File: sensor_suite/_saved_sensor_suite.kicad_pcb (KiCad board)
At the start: 4 copper layers, 12 parts, among them J1 Conn_01x02, J2 Conn_01x02, J3 Bar02, J4 LSM303, U3 MAX6581, U4 ADuM1250, U5 LM3480-3.3

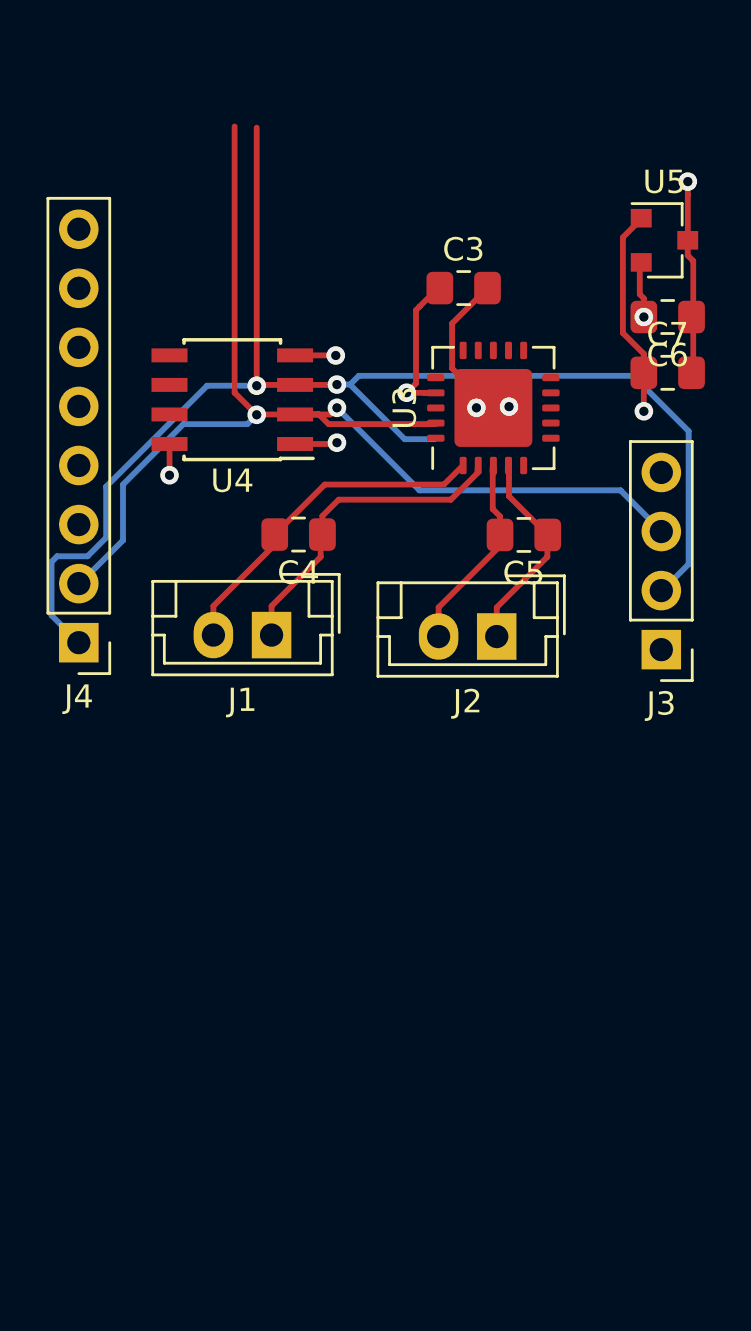
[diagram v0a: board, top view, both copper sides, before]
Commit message: PCA symbol moved to sensor board
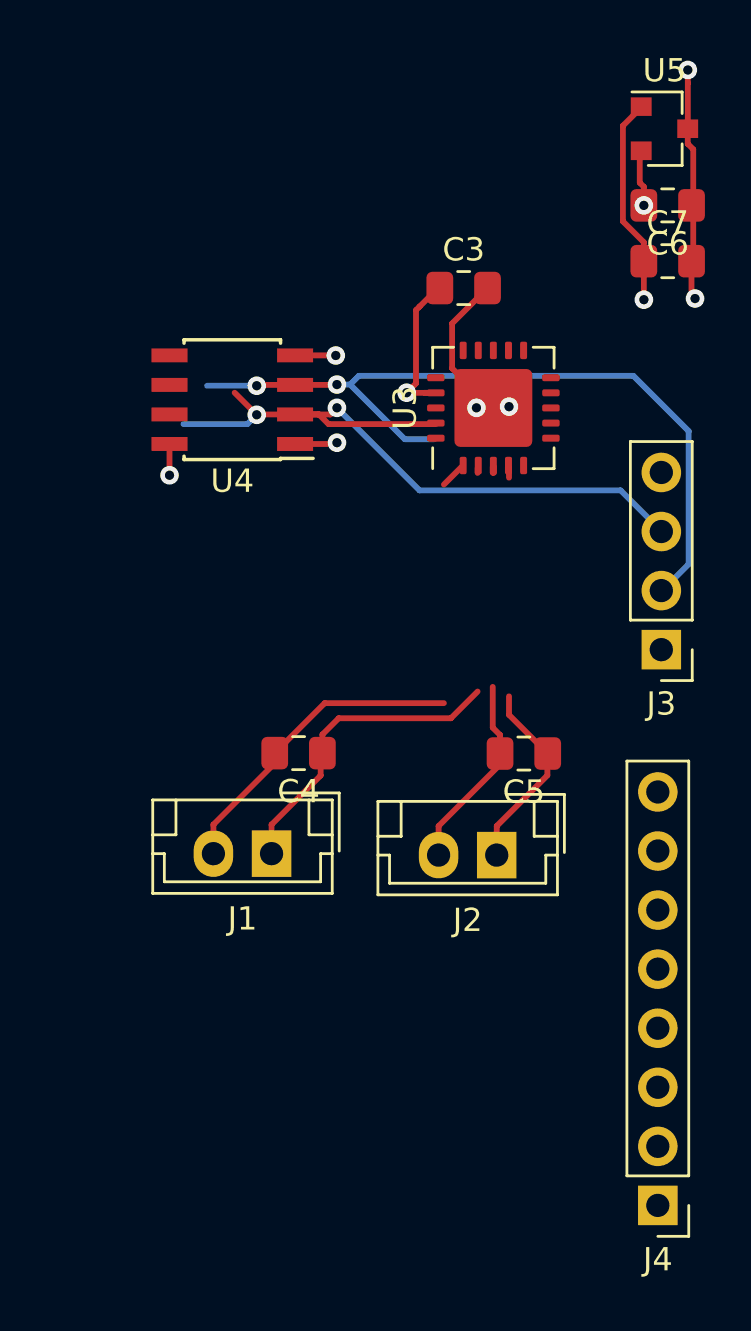
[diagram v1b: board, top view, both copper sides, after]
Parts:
- moved J4 34.7 mm to (170.2, 126.0)
- moved C5 9.40 mm to (164.4, 106.6)
- moved J1 9.40 mm to (153.6, 110.9)
- moved C4 9.40 mm to (154.8, 106.5)
- moved J2 9.40 mm to (163.3, 110.9)
- moved U5 4.80 mm to (170.5, 79.7)
- moved C6 4.80 mm to (170.6, 83.0)
- moved C7 4.80 mm to (170.6, 85.4)
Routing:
- net /SCL1: track 60.0 -> 33.9 mm
- net /SDA1: track 50.9 -> 30.7 mm
- net GND: track 8.47 -> 10.1 mm, vias 1 -> 2

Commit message: updated library
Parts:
- removed C6, C7: 0.1uF, Capacitor_SMD:C_0805_2012Metric_Pad1.15x1.40mm_HandSolder
- removed U3: MAX6581, Package_DFN_QFN:QFN-20-1EP_5x5mm_P0.65mm_EP3.35x3.35mm
- removed U4: ADuM1250, Package_SO:SOIC-8_3.9x4.9mm_P1.27mm
- removed U5: LM3480-3.3, Package_TO_SOT_SMD:SOT-23
- added C1: 100pF, Capacitor_SMD:C_0805_2012Metric_Pad1.15x1.40mm_HandSolder, F.Cu at (122.7, 115.8)
- added C2: 100pF, Capacitor_SMD:C_0805_2012Metric_Pad1.15x1.40mm_HandSolder, F.Cu at (132.7, 115.6)
- added J5: LSM303, rov:LSM303, F.Cu at (94.2, 122.5)
- added U1: MAX6581, Package_DFN_QFN:QFN-20-1EP_5x5mm_P0.65mm_EP3.35x3.35mm, F.Cu at (131.5, 109.1)
- added U2: LM3480-3.3, Package_TO_SOT_SMD:SOT-23, F.Cu at (117.8, 110.1)
- C4, C5: value 100pF -> 0.1uF
- J1: value Conn_01x02 -> Bar02; footprint Connector_JST:JST_EH_B02B-EH-A_1x02_P2.50mm_Vertical -> Connector_PinHeader_2.54mm:PinHeader_1x04_P2.54mm_Vertical
- J2: value Conn_01x02 -> Conn_02x15_Top_Bottom; footprint Connector_JST:JST_EH_B02B-EH-A_1x02_P2.50mm_Vertical -> rov:PCA9685
- J3: value Bar02 -> Conn_01x02; footprint Connector_PinHeader_2.54mm:PinHeader_1x04_P2.54mm_Vertical -> Connector_JST:JST_EH_B02B-EH-A_1x02_P2.50mm_Vertical
- J4: value LSM303 -> Conn_01x02; footprint Connector_PinHeader_2.54mm:PinHeader_1x08_P2.54mm_Vertical -> Connector_JST:JST_EH_B02B-EH-A_1x02_P2.50mm_Vertical
- moved J2 64.2 mm to (105.2, 83.5), turned to 0 degrees
- moved J3 52.3 mm to (121.5, 120.8)
- moved C5 41.3 mm to (123.3, 110.3), turned to 90 degrees
- moved J4 39.1 mm to (131.5, 120.8)
- moved C3 36.2 mm to (130.1, 103.9)
- moved C4 33.9 mm to (121.1, 110.1), turned to 270 degrees
- moved J1 16.2 mm to (137.6, 113.6), turned to 0 degrees
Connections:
- C4 pad 1: /temp1p -> GNDPWR
- C4 pad 2: /temp1n -> +5VP
- C5 pad 1: /temp2p -> +3V3
- C5 pad 2: /temp2n -> GNDPWR
- J1 pad 1: /temp1p -> +3V3
- J1 pad 2: /temp1n -> /SCL_iso
- J2 pad 1: /temp2p -> GND
- J2 pad 2: /temp2n -> Net-(J2-Pad2)
- J3 pad 1: +3V3 -> /temp1p
- J3 pad 2: /SCL1 -> /temp1n
- J4 pad 1: /SCL1 -> /temp2p
- J4 pad 2: /SDA1 -> /temp2n
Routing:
- net +3V3: track 17.6 -> 74.3 mm, vias 3 -> 0
- net /SCL1: track 33.9 -> 0.00 mm, vias 2 -> 0
- net /SDA1: track 30.7 -> 0.00 mm, vias 2 -> 0
- net GND: track 10.1 -> 0.00 mm, vias 2 -> 0
- net GNDPWR: track 0.00 -> 10.1 mm, vias 0 -> 2
- net +12P: track 2.42 -> 0.00 mm, vias 1 -> 0
- net /temp2p: track 9.04 -> 10.9 mm
- net GNDS: track 6.96 -> 5.21 mm, vias 3 -> 2
- net /temp2n: track 8.94 -> 10.7 mm
- net /temp1n: track 14.7 -> 16.4 mm
- net /temp1p: track 13.7 -> 15.0 mm
- net +5VP: track 1.34 -> 2.42 mm
- removed copper zone on power.Cu, net +12P
- removed copper zone on power.Cu, net +3V3
- removed copper zone on power.Cu, net +5VP
- removed copper zone on ground.Cu, net GND
- removed copper zone on ground.Cu, net GNDS

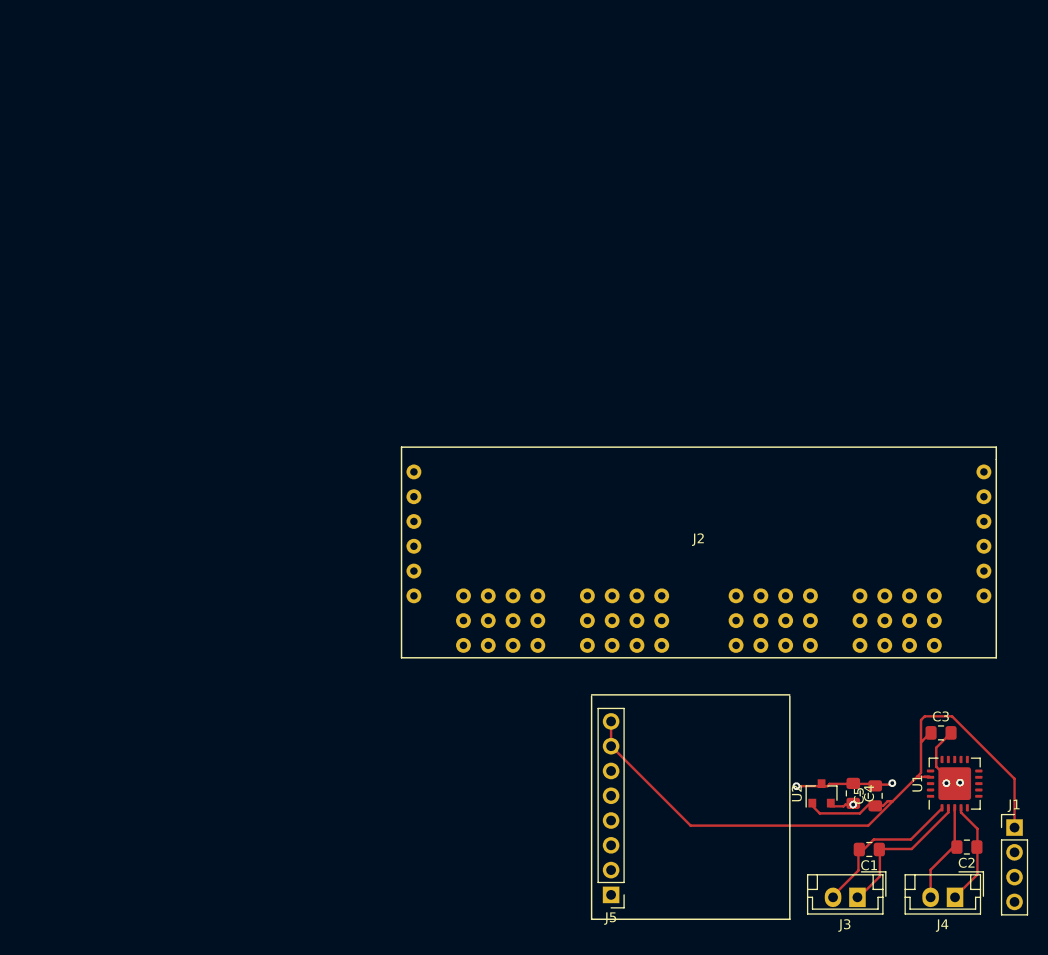
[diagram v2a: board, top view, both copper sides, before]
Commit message: updated ESC's
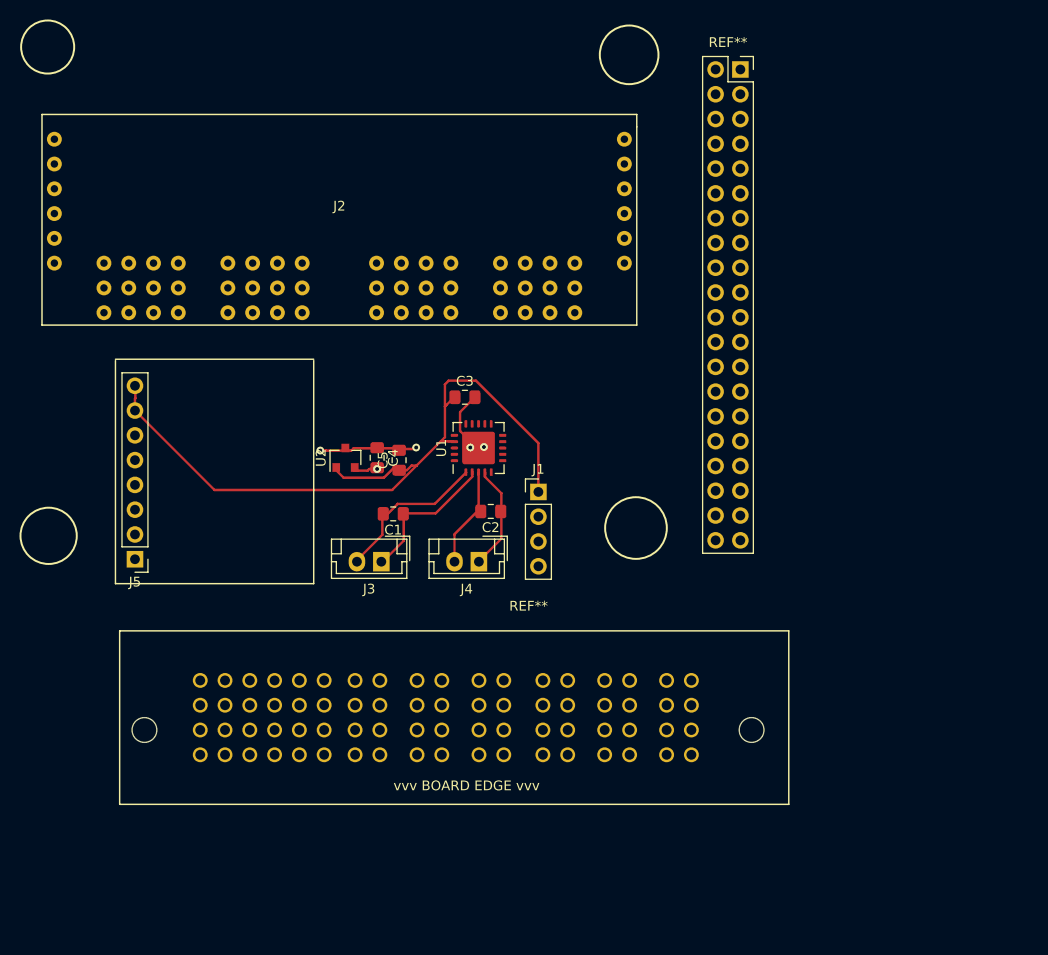
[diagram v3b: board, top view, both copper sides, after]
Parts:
- added REF**: 609-3634-ND, rov:609-3634-ND, F.Cu at (48.4, 98.5)
- added REF**: PinSocket_2x20_P2.54mm_Vertical, Connector_PinSocket_2.54mm:PinSocket_2x20_P2.54mm_Vertical, F.Cu at (109.5, 35.9)
- moved C3 59.7 mm to (81.3, 69.5)
- moved C4 59.7 mm to (72.3, 75.7)
- moved C5 59.7 mm to (74.5, 75.9)
- moved J3 59.7 mm to (72.7, 86.3)
- moved J4 59.7 mm to (82.7, 86.3)
- moved J5 59.7 mm to (45.5, 88.1)
- moved U2 59.7 mm to (69.0, 75.7)
- moved C1 59.7 mm to (73.9, 81.4)
- moved C2 59.7 mm to (83.9, 81.2)
- moved J1 59.7 mm to (88.8, 79.2)
- moved U1 59.7 mm to (82.7, 74.7)
- moved J2 50.2 mm to (68.4, 49.4)

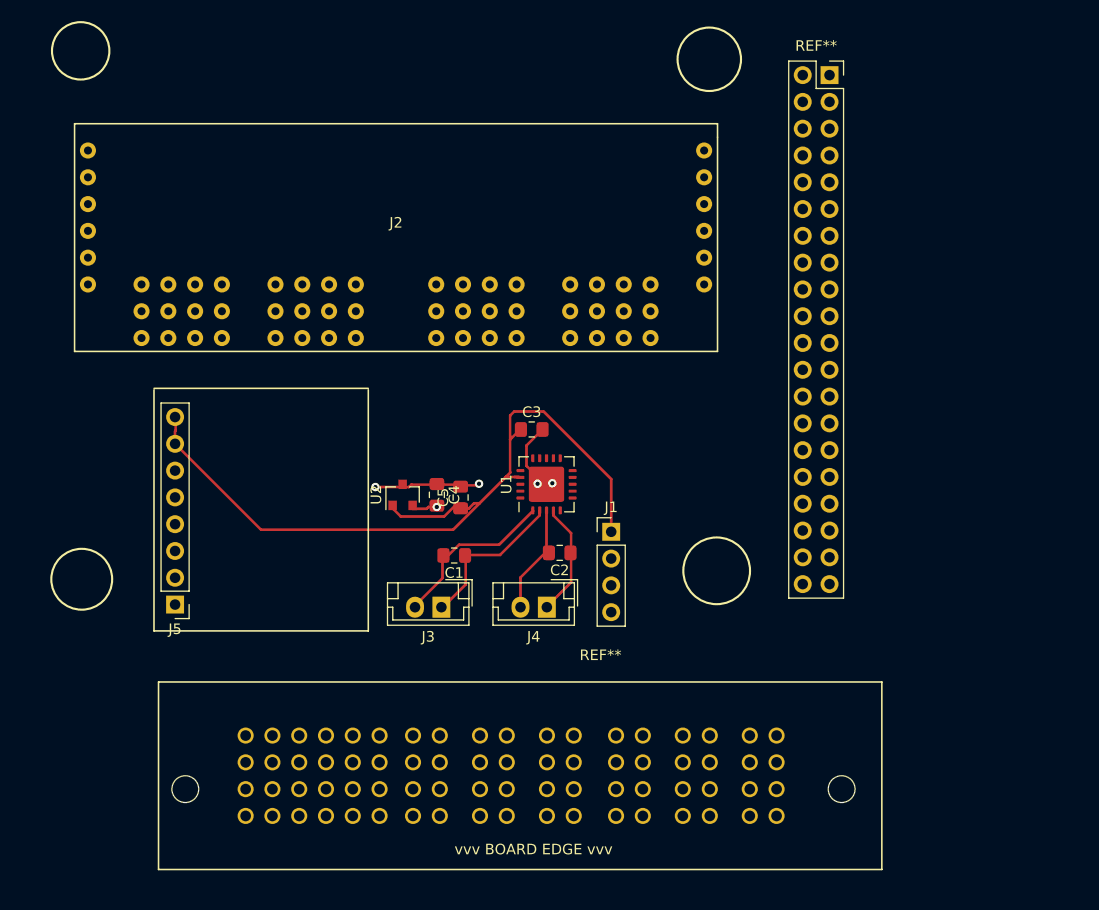
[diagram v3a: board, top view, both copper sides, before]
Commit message: sensors unrouted
nick look in "sensor suite"
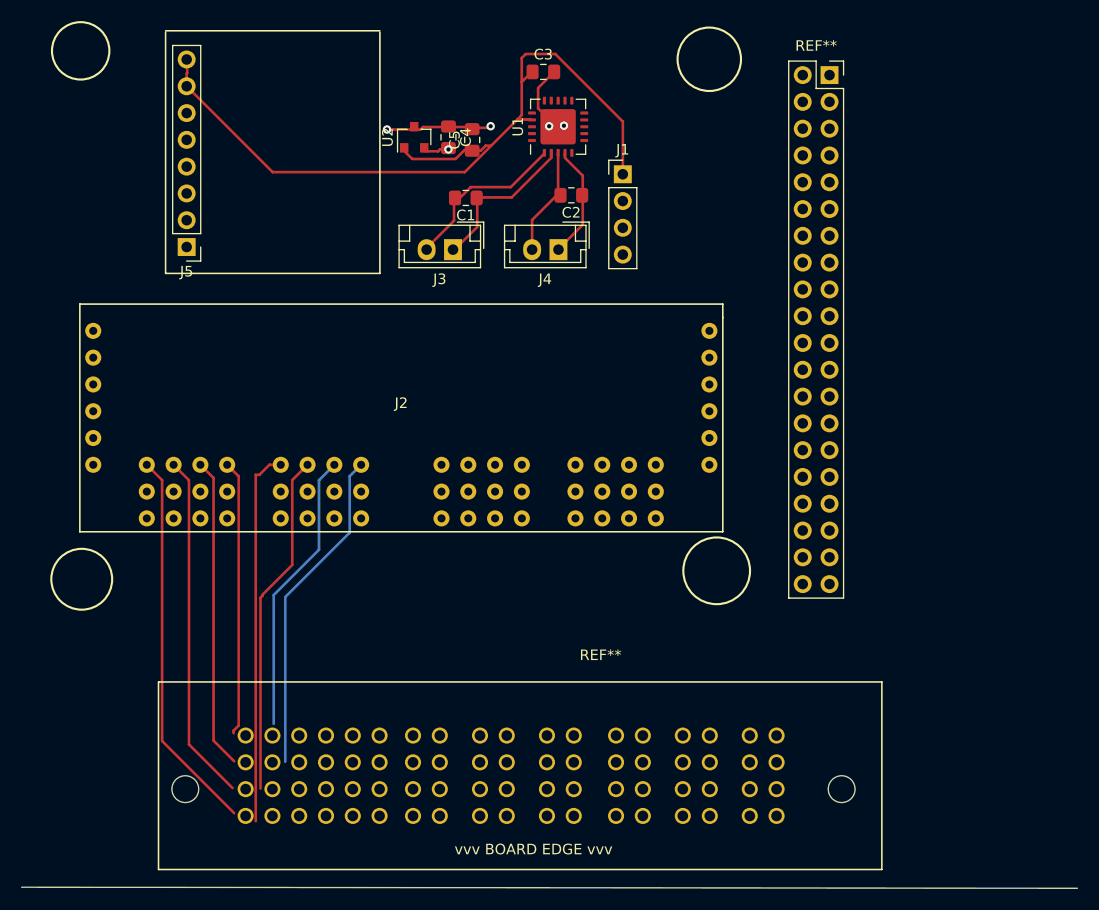
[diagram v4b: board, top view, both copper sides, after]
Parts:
- moved C1 33.9 mm to (75.0, 47.5)
- moved C2 33.9 mm to (85.0, 47.3)
- moved J1 33.9 mm to (89.9, 45.3)
- moved U1 33.9 mm to (83.8, 40.8)
- moved C3 33.9 mm to (82.4, 35.6)
- moved C4 33.9 mm to (73.4, 41.8)
- moved C5 33.9 mm to (75.6, 42.0)
- moved J3 33.9 mm to (73.8, 52.5)
- moved J4 33.9 mm to (83.8, 52.5)
- moved J5 33.9 mm to (46.5, 54.2)
- moved U2 33.9 mm to (70.1, 41.8)
- moved J2 17.1 mm to (68.9, 66.5)
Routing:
- net /PWM5: track 0.00 -> 90.6 mm
- net /PWM0: track 0.00 -> 36.5 mm
- net /PWM4: track 0.00 -> 35.6 mm
- net /PWM1: track 0.00 -> 33.0 mm
- net /PWM2: track 0.00 -> 29.4 mm
- net /PWM3: track 0.00 -> 26.1 mm
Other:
- board outline added: 100.1 x 0.1 mm

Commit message: Sensor Board
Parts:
- removed REF**: 609-3634-ND, rov:609-3634-ND
- removed REF**: PinSocket_2x20_P2.54mm_Vertical, Connector_PinSocket_2.54mm:PinSocket_2x20_P2.54mm_Vertical
- added CN1: 609-3634-ND, ROV:609-3634-ND, F.Cu at (129.9, 141.1)
- added J6: Conn_02x20_Counter_Clockwise, Connector_PinHeader_2.54mm:PinHeader_2x20_P2.54mm_Vertical, F.Cu at (196.5, 83.7)
- J2: value Conn_02x15_Top_Bottom -> Conn_02x10_Counter_Clockwise; footprint rov:PCA9685 -> ROV:PCA9685
- J5: footprint rov:LSM303 -> Connector_PinHeader_2.54mm:PinHeader_1x08_P2.54mm_Vertical
- moved U2 129.2 mm to (182.8, 105.2), turned to 270 degrees
- moved C4 122.0 mm to (177.5, 105.4), turned to 90 degrees
- moved C5 117.8 mm to (174.9, 105.4), turned to 270 degrees
- moved C3 114.0 mm to (168.7, 110.0), turned to 180 degrees
- moved C1 112.7 mm to (176.2, 97.2), turned to 0 degrees
- moved J3 106.8 mm to (175.5, 85.0), turned to 0 degrees
- moved U1 104.4 mm to (166.8, 104.1), turned to 270 degrees
- moved J2 102.5 mm to (158.5, 116.3)
- moved C2 95.6 mm to (166.2, 97.9), turned to 0 degrees
- moved J1 88.5 mm to (159.1, 100.5), turned to 180 degrees
- moved J4 88.2 mm to (165.8, 84.9), turned to 0 degrees
- moved J5 87.8 mm to (129.5, 83.0), turned to 0 degrees
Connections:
- J2 pad 1: GND -> PWM_0
- J2 pad 10: /PWM1 -> PWM_9
- J2 pad 11: +5VP -> PWM_10
- J2 pad 12: GNDPWR -> PWM_11
- J2 pad 13: /PWM2 -> PWM_12
- J2 pad 14: +5VP -> PWM_13
- J2 pad 15: GNDPWR -> PWM_14
- J2 pad 16: /PWM3 -> PWM_15
- J2 pad 17: +5VP -> GNDPWR
- J2 pad 18: GNDPWR -> /SCL_iso
- J2 pad 19: /PWM4 -> /SDA_iso
- J2 pad 2: Net-(J2-Pad2) -> PWM_1
- J2 pad 3: /SCL_iso -> PWM_2
- J2 pad 4: /SDA_iso -> PWM_3
- J2 pad 5: +5VP -> PWM_4
- J2 pad 6: +5VP -> PWM_5
- J2 pad 7: /PWM0 -> PWM_6
- J2 pad 8: +5VP -> PWM_7
- J2 pad 9: GNDPWR -> PWM_8
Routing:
- net /SDA_iso: track 0.00 -> 263.6 mm
- net /SCL_iso: track 0.00 -> 256.9 mm, vias 0 -> 2
- net /PWM5: track 90.6 -> 0.00 mm
- net PWM_12: track 0.00 -> 64.5 mm
- net GNDS: track 5.21 -> 52.4 mm, vias 2 -> 0
- net PWM_14: track 0.00 -> 46.2 mm
- net PWM_15: track 0.00 -> 45.5 mm
- net PWM_13: track 0.00 -> 45.1 mm
- net PWM_8: track 0.00 -> 41.7 mm
- net /PWM0: track 36.5 -> 0.00 mm
- net /PWM4: track 35.6 -> 0.00 mm
- net PWM_9: track 0.00 -> 34.3 mm
- net PWM_10: track 0.00 -> 33.5 mm
- net PWM_11: track 0.00 -> 33.3 mm
- net /PWM1: track 33.0 -> 0.00 mm
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- added copper zone on In1.Cu, net +5VP
- added copper zone on In2.Cu, net GNDPWR
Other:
- board size 100.1 x 0.1 mm -> 78.9 x 74.1 mm
- net class PWM added: clearance 0.1524, trace_width 0.1524, via_dia 0.8, via_drill 0.4
- rule trace_min: 0.2 -> 0.127
- board text added: "anode"
- board text added: "|"
